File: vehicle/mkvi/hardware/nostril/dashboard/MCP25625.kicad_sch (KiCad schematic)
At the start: 9 parts, among them U2 MCP25625-x-SS, Y1 Crystal_8MHz_12pF

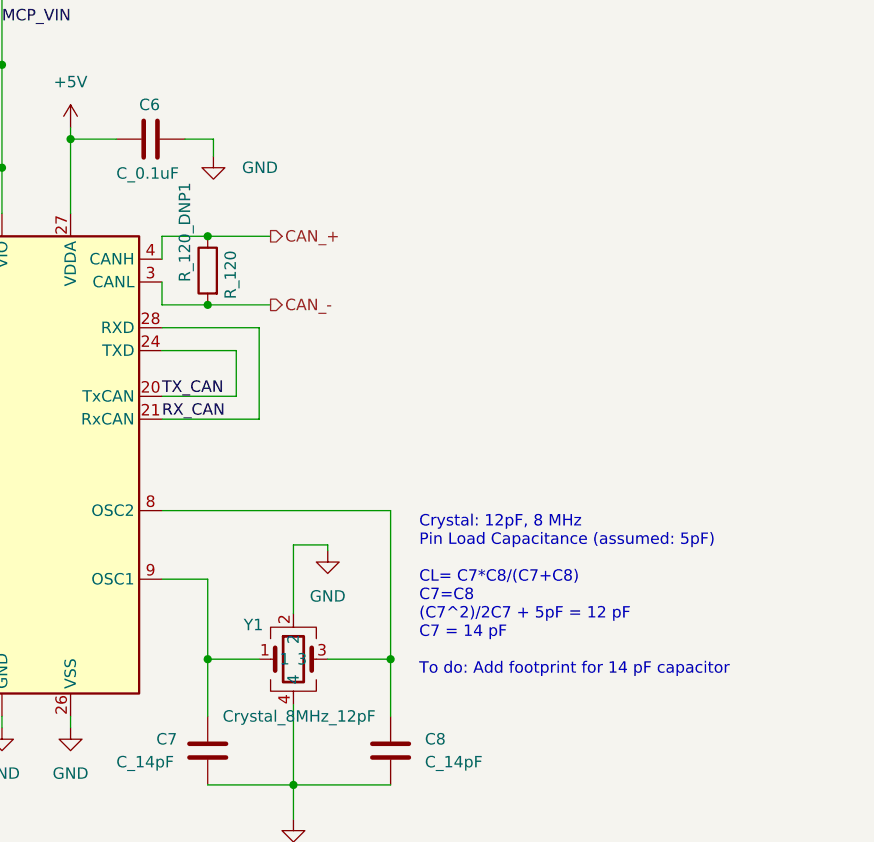
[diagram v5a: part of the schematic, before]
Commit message: Finish rerouting connections
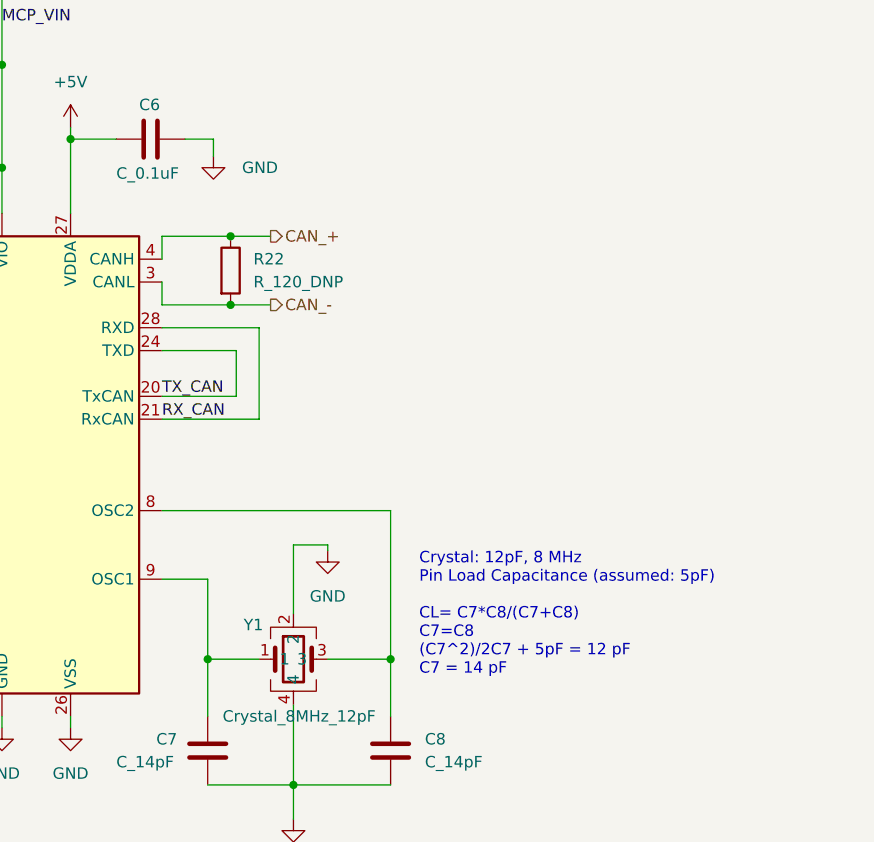
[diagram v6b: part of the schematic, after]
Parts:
- removed R_120_DNP1: R_120, footprints:R_0805_OEM, symbol formula:R_120
- added R22: R_120_DNP, footprints:R_0805_OEM, symbol formula:R_120_DNP
- C4, C5, C6, C7, C8: footprint footprints:C_0805_OEM -> Capacitor_SMD:C_0603_1608Metric_Pad1.08x0.95mm_HandSolder
- R13: footprint footprints:R_0805_OEM -> Resistor_SMD:R_0603_1608Metric_Pad0.98x0.95mm_HandSolder
- Y1: footprint XTAL_ECS-240-8-33-AGN-TR -> footprints:XTAL_ECS-240-8-33-AGN-TR
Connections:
- net CAN_+: now also R22.1
- net CAN_-: now also R22.2
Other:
- note added: "Crystal: 12pF, 8 MHz Pin Load Capacitance (assumed: 5pF) CL= C7*C8/(C7+C8) C7=C8 (C7^2)/2C7 + 5pF = 12 pF C7 = 14 pF"
- note removed: "Crystal: 12pF, 8 MHz Pin Load Capacitance (assumed: 5pF) CL= C7*C8/(C7+C8) C7=C8 (C7^2)/2C7 + 5pF = 12 pF C7 = 14 pF To do: Add footprint for 14 pF capacitor"
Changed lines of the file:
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@@
   (junction (at 151.13 120.015) (diameter 0) (color 0 0 0 0)
   )
-  (junction (at 151.13 80.645) (diameter 0) (color 0 0 0 0)
-  )
   (junction (at 160.655 133.985) (diameter 0) (color 0 0 0 0)
   )
-  (junction (at 151.13 73.025) (diameter 0) (color 0 0 0 0)
+  (junction (at 153.67 80.645) (diameter 0) (color 0 0 0 0)
+  )
+  (junction (at 153.67 73.025) (diameter 0) (color 0 0 0 0)
   )
   (junction (at 135.89 62.23) (diameter 0) (color 0 0 0 0)
@@
     (stroke (width 0) (type default) (color 0 0 0 0))
   )
-  (wire (pts (xy 158.115 73.025) (xy 151.13 73.025))
-    (stroke (width 0) (type default) (color 0 0 0 0))
-  )
   (wire (pts (xy 156.845 83.185) (xy 156.845 93.345))
     (stroke (width 0) (type default) (color 0 0 0 0))
@@
     (stroke (width 0) (type default) (color 0 0 0 0))
   )
-  (wire (pts (xy 151.13 73.025) (xy 146.05 73.025))
-    (stroke (width 0) (type default) (color 0 0 0 0))
-  )
-  (wire (pts (xy 151.13 80.645) (xy 146.05 80.645))
+  (wire (pts (xy 146.05 73.025) (xy 153.67 73.025))
+    (stroke (width 0) (type default) (color 0 0 0 0))
+  )
+  (wire (pts (xy 146.05 80.645) (xy 153.67 80.645))
     (stroke (width 0) (type default) (color 0 0 0 0))
   )
@@
     (stroke (width 0) (type default) (color 0 0 0 0))
   )
+  (wire (pts (xy 153.67 73.025) (xy 158.115 73.025))
+    (stroke (width 0) (type default) (color 0 0 0 0))
+  )
   (wire (pts (xy 171.45 120.015) (xy 164.465 120.015))
     (stroke (width 0) (type default) (color 0 0 0 0))
@@
     (stroke (width 0) (type default) (color 0 0 0 0))
   )
-  (wire (pts (xy 158.115 80.645) (xy 151.13 80.645))
+  (wire (pts (xy 153.67 80.645) (xy 158.115 80.645))
     (stroke (width 0) (type default) (color 0 0 0 0))
   )
@@
     (stroke (width 0) (type default) (color 0 0 0 0))
   )
-  (text "Crystal: 12pF, 8 MHz\nPin Load Capacitance (assumed: 5pF)\n\nCL= C7*C8/(C7+C8)\nC7=C8\n(C7^2)/2C7 + 5pF = 12 pF\nC7 = 14 pF\n\nTo do: Add footprint for 14 pF capacitor"
+  (text "Crystal: 12pF, 8 MHz\nPin Load Capacitance (assumed: 5pF)\n\nCL= C7*C8/(C7+C8)\nC7=C8\n(C7^2)/2C7 + 5pF = 12 pF\nC7 = 14 pF"
     (at 174.625 121.92 0)
     (effects (font (size 1.27 1.27)) (justify left bottom))
@@
     (effects (font (size 1.27 1.27)) (justify right))
   )
+  (symbol (lib_id "formula:R_120_DNP") (at 153.67 76.835 0) (unit 1)
+    (in_bom yes) (on_board yes) (fields_autoplaced)
+    (property "Reference" "R22" (id 0) (at 156.21 75.5649 0)
+      (effects (font (size 1.27 1.27)) (justify left))
+    )
+    (property "Value" "R_120_DNP" (id 1) (at 156.21 78.1049 0)
+      (effects (font (size 1.27 1.27)) (justify left))
+    )
+    (property "Footprint" "footprints:R_0805_OEM" (id 2) (at 123.19 73.025 0)
+      (effects (font (size 1.27 1.27)) (justify left) hide)
+    )
+    (property "Datasheet" "https://www.mouser.com/datasheet/2/315/AOA0000C304-1149620.pdf" (id 3) (at 123.19 65.405 0)
+      (effects (font (size 1.27 1.27)) (justify left) hide)
+    )
+    (property "MFN" "DK" (id 4) (at 153.67 76.835 0)
+      (effects (font (size 1.524 1.524)) hide)
+    )
+    (property "MPN" "667-ERJ-6ENF1200V" (id 5) (at 123.19 70.485 0)
+      (effects (font (size 1.524 1.524)) (justify left) hide)
+    )
+    (property "PurchasingLink" "https://www.mouser.com/ProductDetail/Panasonic-Industrial-Devices/ERJ-6ENF1200V?qs=sGAEpiMZZMvdGkrng054t8AJgcdMkx7x%252bFQnctTMUmU%3d" (id 6) (at 123.19 67.945 0)
+      (effects (font (size 1.524 1.524)) (justify left) hide)
+    )
+    (pin "1")
+    (pin "2")
+  )
   (symbol (lib_id "formula:C_0.1uF") (at 115.57 65.405 270) (mirror x) (unit 1)
     (in_bom yes) (on_board yes)
     (property "Reference" "C5" (id 0) (at 115.57 61.595 90))
     (property "Value" "C_0.1uF" (id 1) (at 115.57 69.215 90))
-    (property "Footprint" "footprints:C_0805_OEM" (id 2) (at 111.76 64.4398 0)
+    (property "Footprint" "Capacitor_SMD:C_0603_1608Metric_Pad1.08x0.95mm_HandSolder" (id 2) (at 111.76 64.4398 0)
       (effects (font (size 1.27 1.27)) hide)
     )
@@
     (property "Reference" "Y1" (id 0) (at 156.21 116.205 0))
     (property "Value" "Crystal_8MHz_12pF" (id 1) (at 161.29 126.365 0))
-    (property "Footprint" "XTAL_ECS-240-8-33-AGN-TR" (id 2) (at 221.615 99.695 0)
+    (property "Footprint" "footprints:XTAL_ECS-240-8-33-AGN-TR" (id 2) (at 221.615 99.695 0)
       (effects (font (size 1.27 1.27)) (justify left bottom) hide)
     )
@@
       (effects (font (size 1.27 1.27)) (justify left))
     )
-    (property "Footprint" "footprints:C_0805_OEM" (id 2) (at 172.4152 133.985 0)
+    (property "Footprint" "Capacitor_SMD:C_0603_1608Metric_Pad1.08x0.95mm_HandSolder" (id 2) (at 172.4152 133.985 0)
       (effects (font (size 1.27 1.27)) hide)
     )
@@
       (effects (font (size 1.27 1.27)) (justify left))
     )
-    (property "Footprint" "footprints:C_0805_OEM" (id 2) (at 140.97 63.1952 0)
+    (property "Footprint" "Capacitor_SMD:C_0603_1608Metric_Pad1.08x0.95mm_HandSolder" (id 2) (at 140.97 63.1952 0)
       (effects (font (size 1.27 1.27)) hide)
     )
@@
       (effects (font (size 1.27 1.27)) (justify left))
     )
-    (property "Footprint" "footprints:C_0805_OEM" (id 2) (at 111.76 54.9402 0)
+    (property "Footprint" "Capacitor_SMD:C_0603_1608Metric_Pad1.08x0.95mm_HandSolder" (id 2) (at 111.76 54.9402 0)
       (effects (font (size 1.27 1.27)) hide)
     )
@@
     (property "Reference" "R13" (id 0) (at 87.63 87.63 90))
     (property "Value" "R_10K" (id 1) (at 87.63 90.17 90))
-    (property "Footprint" "footprints:R_0805_OEM" (id 2) (at 87.63 95.123 0)
+    (property "Footprint" "Resistor_SMD:R_0603_1608Metric_Pad0.98x0.95mm_HandSolder" (id 2) (at 87.63 95.123 0)
       (effects (font (size 1.27 1.27)) hide)
     )
@@
       (effects (font (size 1.27 1.27)) (justify left))
     )
-    (property "Footprint" "footprints:C_0805_OEM" (id 2) (at 152.0952 133.985 0)
+    (property "Footprint" "Capacitor_SMD:C_0603_1608Metric_Pad1.08x0.95mm_HandSolder" (id 2) (at 152.0952 133.985 0)
       (effects (font (size 1.27 1.27)) hide)
     )
@@
     (pin "1")
   )
-  (symbol (lib_id "formula:R_120") (at 151.13 76.835 0) (mirror y) (unit 1)
-    (in_bom yes) (on_board yes)
-    (property "Reference" "R_120_DNP1" (id 0) (at 148.59 78.105 90)
-      (effects (font (size 1.27 1.27)) (justify left))
-    )
-    (property "Value" "R_120" (id 1) (at 153.67 80.01 90)
-      (effects (font (size 1.27 1.27)) (justify left))
-    )
-    (property "Footprint" "footprints:R_0805_OEM" (id 2) (at 181.61 73.025 0)
-      (effects (font (size 1.27 1.27)) (justify left) hide)
-    )
-    (property "Datasheet" "https://www.mouser.com/datasheet/2/315/AOA0000C304-1149620.pdf" (id 3) (at 181.61 65.405 0)
-      (effects (font (size 1.27 1.27)) (justify left) hide)
-    )
-    (property "MFN" "DK" (id 4) (at 151.13 76.835 0)
-      (effects (font (size 1.524 1.524)) hide)
-    )
-    (property "MPN" "667-ERJ-6ENF1200V" (id 5) (at 181.61 70.485 0)
-      (effects (font (size 1.524 1.524)) (justify left) hide)
-    )
-    (property "PurchasingLink" "https://www.mouser.com/ProductDetail/Panasonic-Industrial-Devices/ERJ-6ENF1200V?qs=sGAEpiMZZMvdGkrng054t8AJgcdMkx7x%252bFQnctTMUmU%3d" (id 6) (at 181.61 67.945 0)
-      (effects (font (size 1.524 1.524)) (justify left) hide)
-    )
-    (pin "1")
-    (pin "2")
-  )
   (symbol (lib_id "power:GND") (at 164.465 107.95 0) (mirror y) (unit 1)

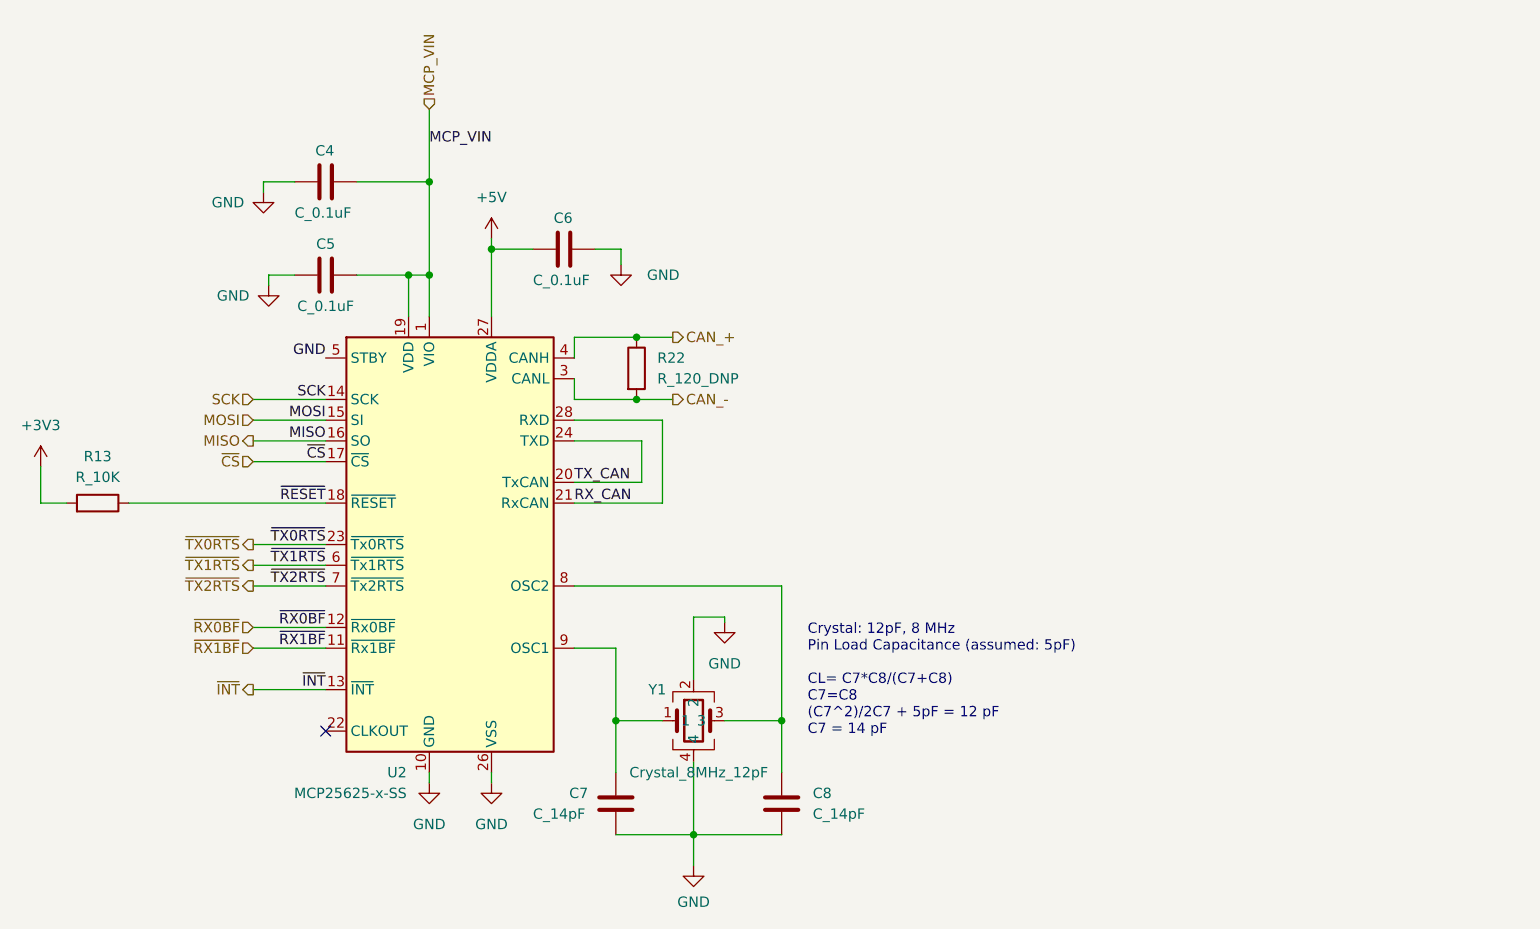
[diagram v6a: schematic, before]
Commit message: Finalize boards for fab (#217)
* add BOM tool to join BOMs

* add custom BOM script for working with custom BOM fields

* add patched QR plugin for better QR codes

* add logo and authors to boards

* update parts library and fix misc issues

* migrate projects to new parts library
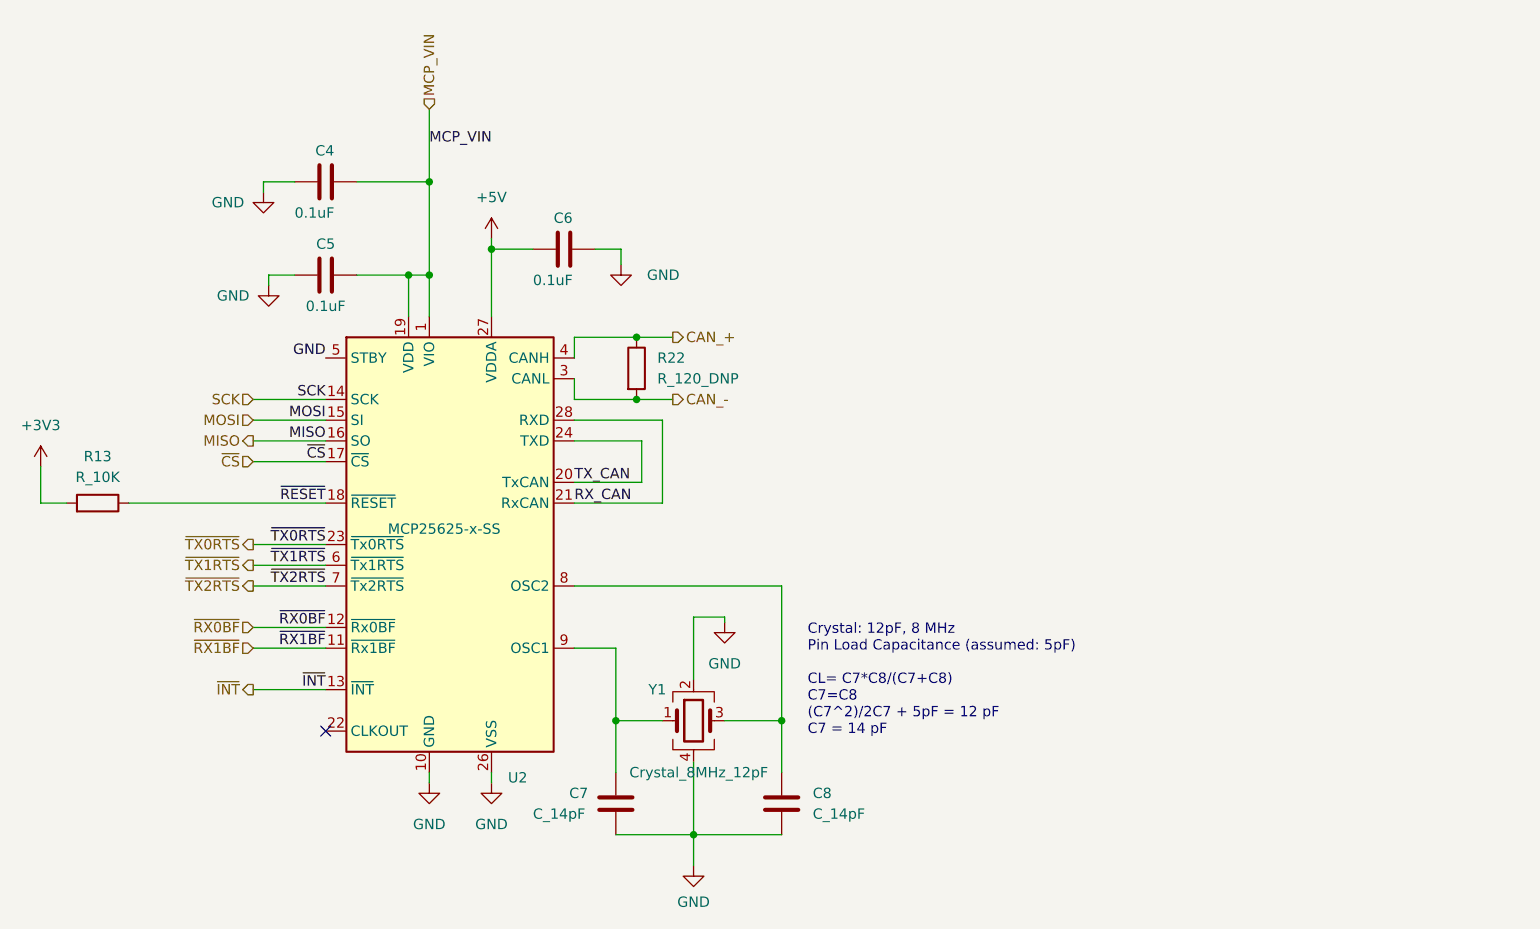
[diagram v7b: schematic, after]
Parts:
- C4, C5, C6: value C_0.1uF -> 0.1uF; footprint Capacitor_SMD:C_0603_1608Metric_Pad1.08x0.95mm_HandSolder -> OEM:C_0603; symbol formula:C_0.1uF -> OEM:0u1F; DKPN (none) -> 1276-1935-2-ND; MFN DK -> Samsung Electro-Mechanics; MPN 478-3352-1-ND -> CL10B104KB8NNWC; NewDesigns (none) -> YES; Package (none) -> 0603; PurchasingLink https://www.digikey.com/products/en?keywords=478-3352-1-ND -> (none); Stocked (none) -> Reel; Style (none) -> SMD
- C7, C8: footprint Capacitor_SMD:C_0603_1608Metric_Pad1.08x0.95mm_HandSolder -> Capacitor_SMD:C_0805_2012Metric; symbol formula:C_14pF -> OEM:14pF; DKPN (none) -> 490-GQM2195C2E140JB12DCT-ND; MFN Murata Electronics -> Murata; NewDesigns (none) -> YES; Package (none) -> 0805; Purchasing Link https://www.digikey.com/en/products/detail/murata-electroni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 -> (none); PurchasingLink https://www.digikey.com/products/en?keywords=478-3352-1-ND -> (none); Stocked (none) -> Tape; Style (none) -> SMD
- R13: footprint Resistor_SMD:R_0603_1608Metric_Pad0.98x0.95mm_HandSolder -> OEM:R_0603; symbol formula:R_10K -> OEM:10KR; DKPN (none) -> RMCF0603FT10K0TR-ND; MFN DK -> Stackpole Electronics; MPN CRS0805-FX-1002ELFCT-ND -> RMCF0603FT10K0; NewDesigns (none) -> YES; Package (none) -> 0603; PurchasingLink https://www.digikey.com/products/en?keywords=CRS0805-FX-100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 -> (none); Stocked (none) -> Reel; Style (none) -> SMD
- R22: footprint footprints:R_0805_OEM -> OEM:R_0603; symbol formula:R_120_DNP -> OEM:120R_DNP; DKPN (none) -> 13-RC0603FR-13120RLDKR-ND; MFN DK -> Yageo; MPN 667-ERJ-6ENF1200V -> RC0603FR-13120RL; NewDesigns (none) -> YES; Package (none) -> 0603; PurchasingLink https://www.mouser.com/ProductDetail/Panasonic-Industrial-D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 -> (none); Stocked (none) -> Digi-Reel; Style (none) -> SMD
- U2: symbol formula:MCP25625-x-SS -> OEM:MCP25625-x-SS; DKPN (none) -> MCP25625T-E/SSCT-ND; MFN DK -> Microchip; MPN MCP25625-E/SS-ND -> MCP25625; NewDesigns (none) -> CHECK STOCK FIRST; Package (none) -> SSOP-28; PurchasingLink https://www.digikey.com/product-detail/en/microchip-technol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 -> (none); Stocked (none) -> Tape; Style (none) -> SMD
- Y1: footprint footprints:XTAL_ECS-240-8-33-AGN-TR -> OEM:ECX-32; symbol formula:Crystal_8MHz_12pF -> OEM:Crystal_8MHz_12pF; AVAILABILITY Good -> (none); DKPN (none) -> 50-ECS-80-12-33-JGN-CT-ND; MF ECS INC -> (none); MFN (none) -> ECS International; MP ECS-80-12-33-JGN-TR -> (none); MPN (none) -> ECS-80-12-33-JGN-TR; NewDesigns (none) -> YES; PACKAGE SMD-4 ECX -> (none); Package (none) -> ECX-32; STANDARD Manufacturer recommendations -> (none); Stocked (none) -> Tape; Style (none) -> SMD
